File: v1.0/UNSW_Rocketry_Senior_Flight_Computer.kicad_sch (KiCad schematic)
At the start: 21 parts, among them U1 STM32L452RETx, Y1 8MHz

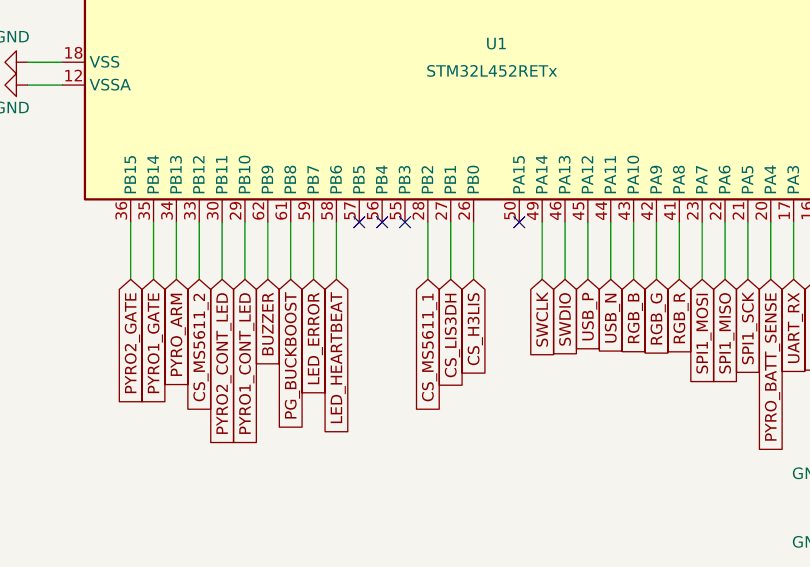
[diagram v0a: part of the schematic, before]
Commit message: v1.0: update schematics and PCB layout
Co-Authored-By: Claude Opus 4.7 (1M context) <noreply@anthropic.com>
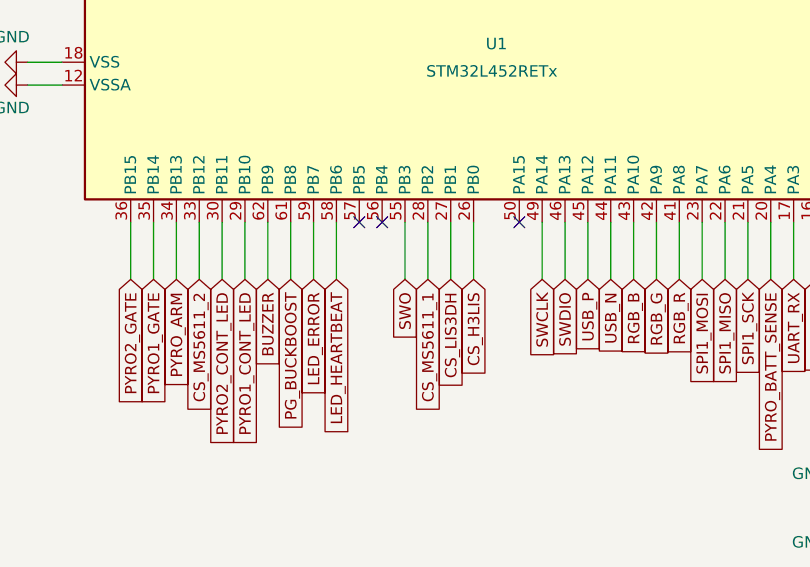
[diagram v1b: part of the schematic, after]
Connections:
- net SWO: now reaches U1.55 (PB3)
- no-connect marks 10 -> 9
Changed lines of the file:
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@@
-	)
-	(no_connect
-		(at 125.73 106.68)
 	)
 	(no_connect
@@
 	(wire
 		(pts
+			(xy 125.73 106.68) (xy 125.73 113.03)
+		)
+		(stroke
+			(width 0)
+			(type default)
+		)
+	)
+	(wire
+		(pts
 			(xy 115.57 106.68) (xy 115.57 113.03)
 		)
@@
 			(hide yes)
 			(show_name no)
+			(do_not_autoplace no)
+			(effects
+				(font
+					(size 1.27 1.27)
+				)
+				(justify right)
+			)
+		)
+	)
+	(global_label "SWO"
+		(shape input)
+		(at 125.73 113.03 270)
+		(fields_autoplaced yes)
+		(effects
+			(font
+				(size 1.27 1.27)
+			)
+			(justify right)
+		)
+		(property "Intersheetrefs" "${INTERSHEET_REFS}"
+			(at 125.73 120.0066 90)
+			(hide yes)
+			(show_name no)
